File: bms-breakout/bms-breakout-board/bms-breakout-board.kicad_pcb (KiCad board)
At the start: 2 copper layers, 66 x 73.7 mm, 7 parts, among them J1 Conn_01x04, J2 Conn_01x04, J3 Conn_01x04, J4 Conn_01x04, J5 Conn_01x04, J6 Conn_01x04, J7 Conn_01x11

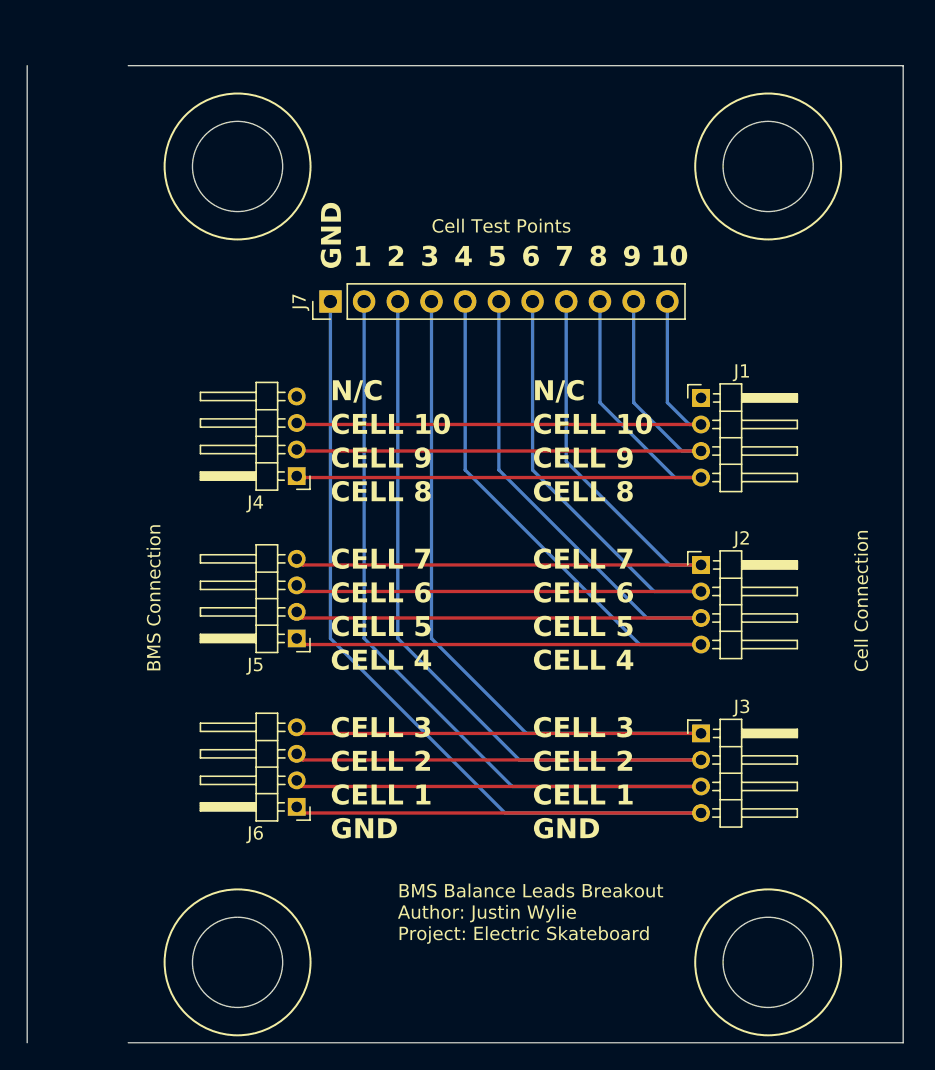
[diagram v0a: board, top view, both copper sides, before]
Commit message: cell balancing breakout board layout pretty much done
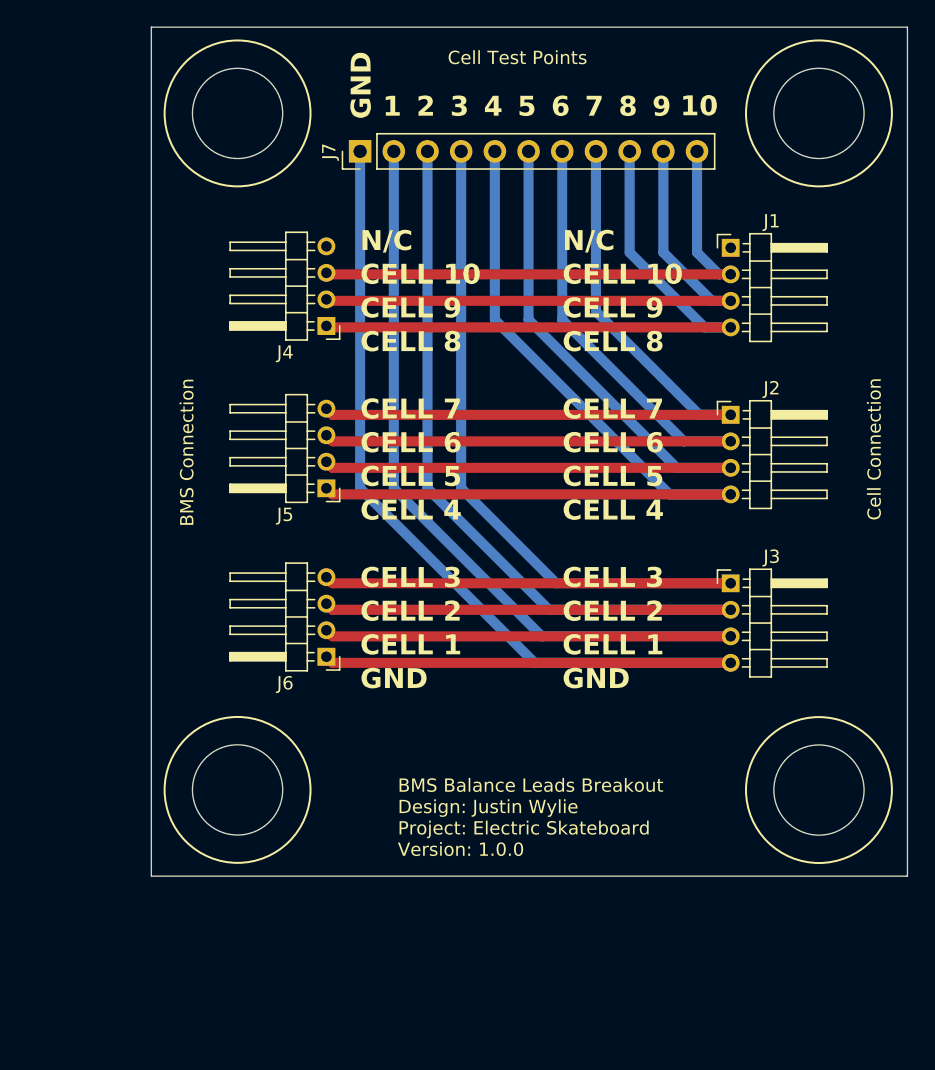
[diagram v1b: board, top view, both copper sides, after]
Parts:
- moved J3 11.5 mm to (93.7, 127.9)
- moved J5 11.5 mm to (63.2, 120.8)
- moved J1 11.5 mm to (93.7, 102.6)
- moved J2 11.5 mm to (93.7, 115.2)
- moved J4 11.5 mm to (63.2, 108.5)
- moved J6 11.5 mm to (63.2, 133.5)
- moved J7 11.5 mm to (65.7, 95.4)
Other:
- board size 66 x 73.7 mm -> 57 x 64 mm
- board text added: "BMS Balance Leads Breakout Design: Justin Wylie Project: Electric Skateboard Version: 1.0.0"
- board text removed: "BMS Balance Leads Breakout Author: Justin Wylie Project: Electric Skateboard"

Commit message: finished v1.0.0 of bms breakout
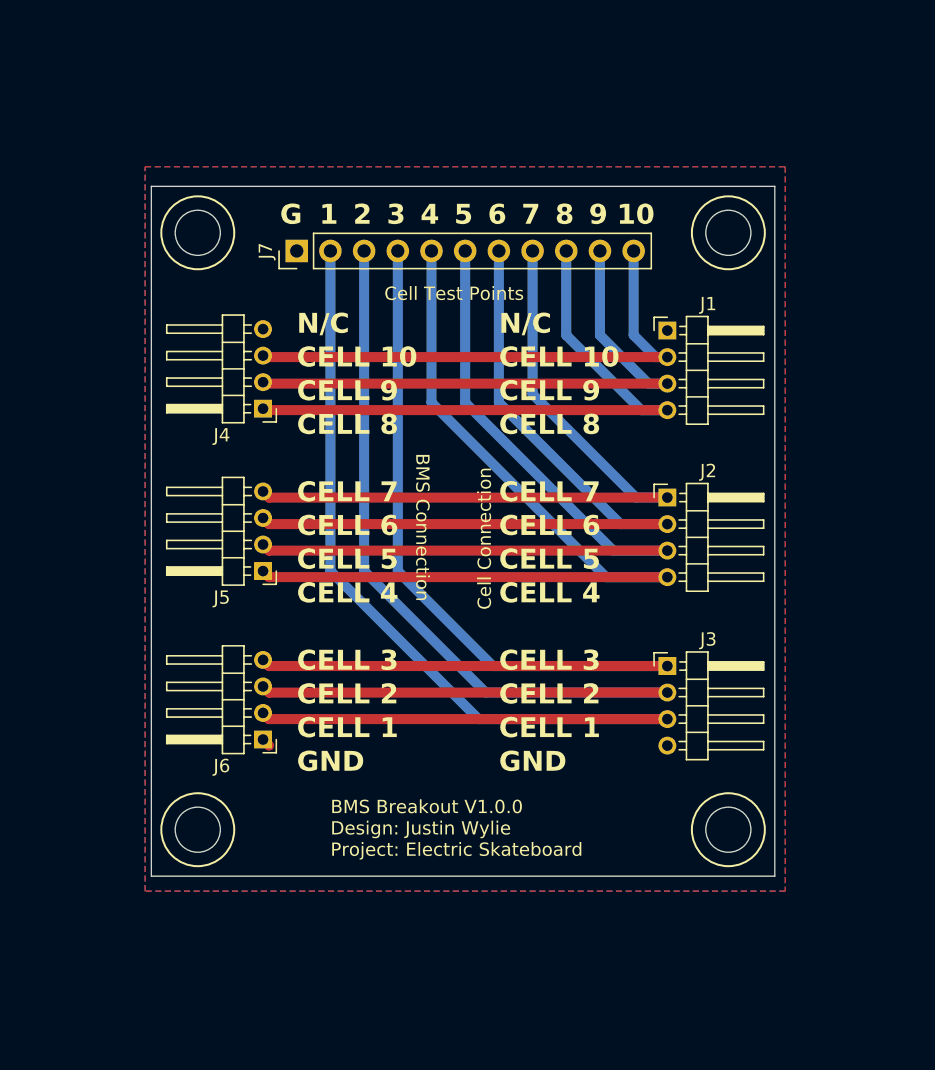
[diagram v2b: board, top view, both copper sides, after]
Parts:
- moved J7 8.90 mm to (61.0, 102.9)
- moved J1 7.86 mm to (88.9, 108.9)
- moved J3 7.86 mm to (88.9, 134.2)
- moved J4 7.86 mm to (58.4, 114.8)
- moved J5 7.86 mm to (58.4, 127.0)
- moved J2 7.86 mm to (88.9, 121.5)
- moved J6 7.86 mm to (58.4, 139.7)
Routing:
- net GND: track 89.5 -> 0.65 mm
- net /cell_7: track 56.1 -> 54.9 mm
- net /cell_6: track 59.9 -> 58.6 mm
- net /cell_5: track 63.2 -> 62.0 mm
- net /cell_4: track 66.6 -> 65.3 mm
- net /cell_1: track 86.1 -> 84.8 mm
- net /cell_8: track 48.1 -> 46.8 mm
- net /cell_3: track 79.4 -> 78.1 mm
- net /cell_2: track 82.7 -> 81.5 mm
- net /cell_10: track 41.4 -> 40.1 mm
- net /cell_9: track 44.7 -> 43.5 mm
- added copper zone on B.Cu, net GND
- added copper zone on F.Cu, net GND
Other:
- board size 57 x 64 mm -> 47 x 52 mm
- board text added: "BMS Breakout V1.0.0 Design: Justin Wylie Project: Electric Skateboard"
- board text added: "G"
- board text removed: "BMS Balance Leads Breakout Design: Justin Wylie Project: Electric Skateboard Version: 1.0.0"
